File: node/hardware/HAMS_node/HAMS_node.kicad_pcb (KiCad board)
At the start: 2 copper layers, 47.5 x 50 mm, 45 parts, among them J1 Conn_01x02, J2 Conn_02x07_Odd_Even, J3 Conn_01x08, J4 Conn_01x04, J5 Conn_01x04, J6 Conn_01x04, J7 Conn_01x04, Q1 DMP3099L, SW1 TL3305BF100QG, SW2 JS202011SCQN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

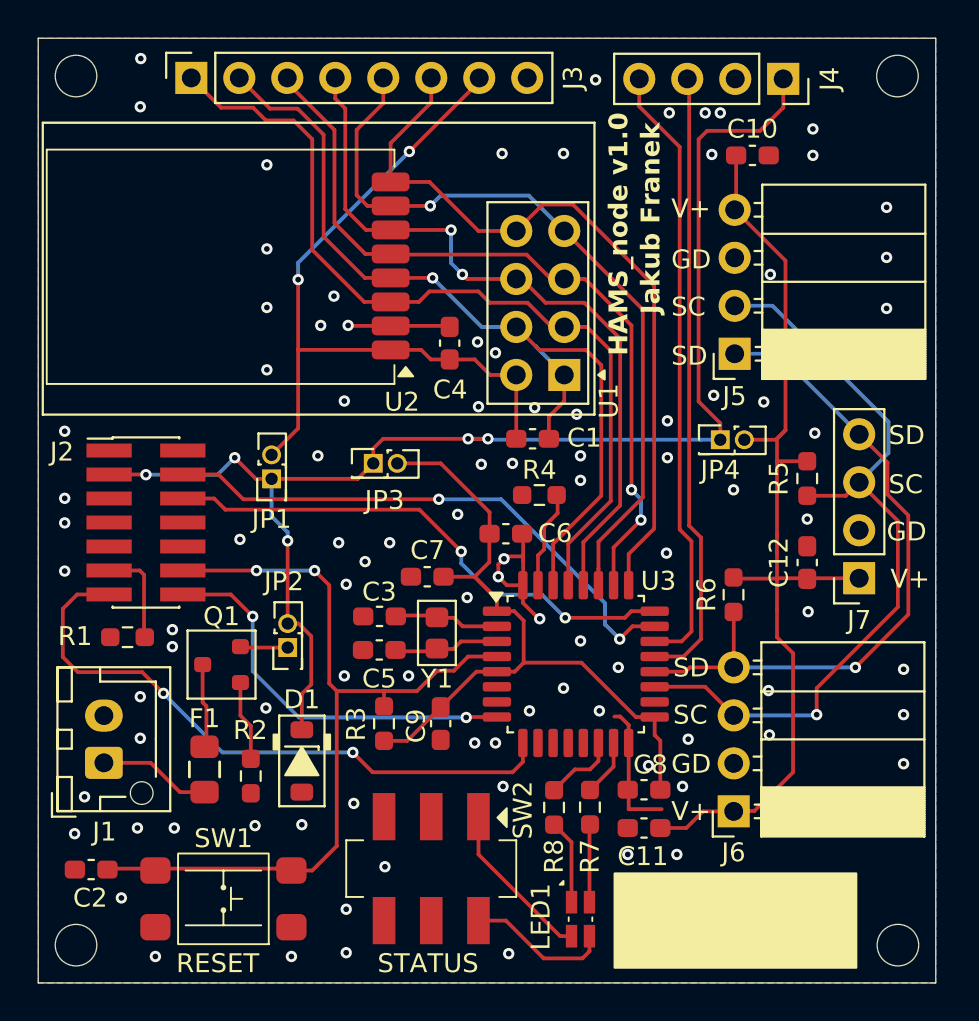
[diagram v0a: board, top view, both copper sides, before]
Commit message: Improve HAMS hub & node HW: schematic and PCB
Finalize hub and node PCB layouts & schematics.
Update task list.
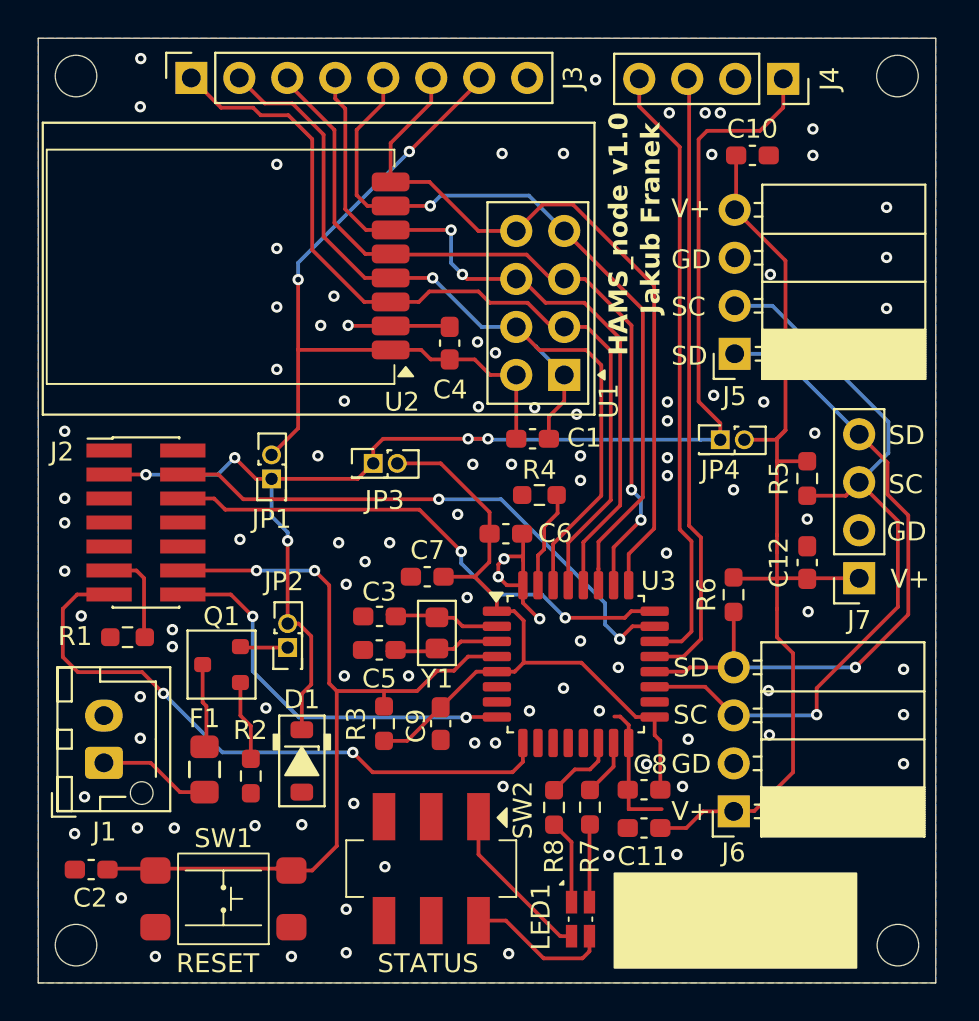
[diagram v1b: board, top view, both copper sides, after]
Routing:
- net GND: vias 95 -> 98
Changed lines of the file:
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@@
 	)
 	(via
-		(at 198.9 96.1)
+		(at 198.8 96.025)
 		(size 0.6)
 		(drill 0.3)
@@
 	)
 	(via
+		(at 199.9 76.85)
+		(size 0.6)
+		(drill 0.3)
+		(layers "F.Cu" "B.Cu")
+		(free yes)
+		(net 1)
+	)
+	(via
 		(at 211.5 71.9)
 		(size 0.6)
@@
 	)
 	(via
-		(at 191.7 80.1)
+		(at 191.65 80.15)
 		(size 0.6)
 		(drill 0.3)
@@
 	)
 	(via
+		(at 199.9 80.75)
+		(size 0.6)
+		(drill 0.3)
+		(layers "F.Cu" "B.Cu")
+		(free yes)
+		(net 1)
+	)
+	(via
 		(at 195.3 89.5)
 		(size 0.6)
@@
 	)
 	(via
-		(at 197.8 100.8)
+		(at 196.8 100.85)
 		(size 0.6)
 		(drill 0.3)
@@
 	)
 	(via
-		(at 178.7 68.75)
+		(at 179.225 68.725)
 		(size 0.6)
 		(drill 0.3)
@@
 	)
 	(via
+		(at 168.875 88.175)
+		(size 0.6)
+		(drill 0.3)
+		(layers "F.Cu" "B.Cu")
+		(free yes)
+		(net 1)
+	)
+	(via
 		(at 194.4 63.7)
 		(size 0.6)
@@
 	)
 	(via
-		(at 190.05 80.15)
+		(at 189.6 80.15)
 		(size 0.6)
 		(drill 0.3)
@@
 	)
 	(via
-		(at 178.7 64.3)
+		(at 179.225 64.275)
 		(size 0.6)
 		(drill 0.3)
@@
 	)
 	(via
-		(at 178.7 71.85)
+		(at 179.225 71.825)
 		(size 0.6)
 		(drill 0.3)
@@
 	)
 	(via
-		(at 178.7 75.15)
+		(at 179.225 75.125)
 		(size 0.6)
 		(drill 0.3)
@@
 	)
 	(segment
-		(start 170.35 85.77)
-		(end 171.97 85.77)
+		(start 172.2 86.175)
+		(end 172.2 88.875)
 		(width 0.2)
 		(layer "F.Cu")
@@
 	)
 	(segment
-		(start 171.97 85.77)
-		(end 172.2 86)
+		(start 171.795 85.77)
+		(end 172.2 86.175)
 		(width 0.2)
 		(layer "F.Cu")
@@
 	)
 	(segment
-		(start 172.2 86)
-		(end 172.2 88.875)
+		(start 170.35 85.77)
+		(end 171.795 85.77)
 		(width 0.2)
 		(layer "F.Cu")
@@
 	)
 	(segment
-		(start 183.885 70.285)
-		(end 181.702 68.102)
-		(width 0.2)
-		(layer "F.Cu")
-		(net 26)
-	)
-	(segment
 		(start 191.8995 72.88)
 		(end 193.1195 74.1)
@@
 	)
 	(segment
-		(start 181.702 62.702)
-		(end 180.325 61.325)
+		(start 181.702 68.102)
+		(end 181.702 62.702)
 		(width 0.2)
 		(layer "F.Cu")
@@
 	)
 	(segment
-		(start 181.702 68.102)
-		(end 181.702 62.702)
-		(width 0.2)
-		(layer "F.Cu")
-		(net 26)
-	)
-	(segment
 		(start 195.6 74.1)
 		(end 196.4 74.9)
@@
 	)
 	(segment
-		(start 180.325 61.325)
-		(end 178.865 61.325)
+		(start 185.25 70.285)
+		(end 183.885 70.285)
 		(width 0.2)
 		(layer "F.Cu")
@@
 	)
 	(segment
+		(start 181.702 62.702)
+		(end 180.05 61.05)
+		(width 0.2)
+		(layer "F.Cu")
+		(net 26)
+	)
+	(segment
 		(start 196.4 81.813928)
 		(end 193.85 84.363928)
@@
 	)
 	(segment
-		(start 177.24 59.7)
-		(end 177.21 59.73)
+		(start 178.59 61.05)
+		(end 177.24 59.7)
 		(width 0.2)
 		(layer "F.Cu")
@@
 	)
 	(segment
-		(start 185.25 70.285)
-		(end 183.885 70.285)
+		(start 183.885 70.285)
+		(end 181.702 68.102)
 		(width 0.2)
 		(layer "F.Cu")
@@
 	)
 	(segment
-		(start 178.865 61.325)
-		(end 177.24 59.7)
+		(start 180.05 61.05)
+		(end 178.59 61.05)
+		(width 0.2)
+		(layer "F.Cu")
+		(net 26)
+	)
+	(segment
+		(start 177.24 59.7)
+		(end 177.21 59.73)
 		(width 0.2)
 		(layer "F.Cu")
@@
 	)
 	(segment
-		(start 199.2 83.55)
-		(end 197.85 84.9)
+		(start 194.9 66.4)
+		(end 199.2 70.7)
 		(width 0.2)
 		(layer "F.Cu")
@@
 	)
 	(segment
-		(start 191.8995 67.8)
-		(end 193.2995 66.4)
+		(start 189.9 67.8)
+		(end 191.8995 67.8)
 		(width 0.2)
 		(layer "F.Cu")
@@
 	)
 	(segment
-		(start 194.9 66.4)
-		(end 199.2 70.7)
+		(start 185.25 63.15)
+		(end 187.4 61)
 		(width 0.2)
 		(layer "F.Cu")
@@
 	)
 	(segment
-		(start 189.9 67.8)
-		(end 191.8995 67.8)
+		(start 185.25 65.205)
+		(end 185.25 63.15)
 		(width 0.2)
 		(layer "F.Cu")
@@
 	)
 	(segment
-		(start 185.25 63.15)
-		(end 187.4 61)
+		(start 187.305 65.205)
+		(end 189.9 67.8)
 		(width 0.2)
 		(layer "F.Cu")
@@
 	)
 	(segment
-		(start 193.2995 66.4)
-		(end 194.9 66.4)
+		(start 187.4 61)
+		(end 187.4 59.7)
 		(width 0.2)
 		(layer "F.Cu")
@@
 	)
 	(segment
-		(start 185.25 65.205)
-		(end 185.25 63.15)
+		(start 191.8995 67.8)
+		(end 193.2995 66.4)
 		(width 0.2)
 		(layer "F.Cu")
@@
 	)
 	(segment
-		(start 187.305 65.205)
-		(end 189.9 67.8)
+		(start 185.25 65.205)
+		(end 187.305 65.205)
 		(width 0.2)
 		(layer "F.Cu")
@@
 	)
 	(segment
-		(start 187.4 61)
-		(end 187.4 59.7)
+		(start 193.2995 66.4)
+		(end 194.9 66.4)
 		(width 0.2)
 		(layer "F.Cu")
@@
 	)
 	(segment
-		(start 185.25 65.205)
-		(end 187.305 65.205)
+		(start 199.2 83.55)
+		(end 197.85 84.9)
 		(width 0.2)
 		(layer "F.Cu")
@@
 	)
 	(segment
+		(start 194.65 84.3)
+		(end 194.65 86.55)
+		(width 0.2)
+		(layer "F.Cu")
+		(net 29)
+	)
+	(segment
 		(start 194.4395 72.88)
 		(end 193.78 72.88)
@@
 	)
 	(segment
-		(start 176.275 61.275)
-		(end 174.7 59.7)
+		(start 186.745 71.555)
+		(end 185.25 71.555)
 		(width 0.2)
 		(layer "F.Cu")
@@
 	)
 	(segment
-		(start 178.65 61.95)
+		(start 178.375 61.675)
 		(end 177.975 61.275)
 		(width 0.2)
@@
 	)
 	(segment
-		(start 186.745 71.555)
-		(end 185.25 71.555)
+		(start 183.855 71.555)
+		(end 181.1 68.8)
 		(width 0.2)
 		(layer "F.Cu")
@@
 	)
 	(segment
-		(start 196.9 74.138419)
-		(end 196.9 82.1)
+		(start 176.275 61.275)
+		(end 174.7 59.7)
 		(width 0.2)
 		(layer "F.Cu")
@@
 	)
 	(segment
-		(start 183.855 71.555)
-		(end 181.1 68.8)
+		(start 181.1 68.8)
+		(end 181.1 62.9375)
 		(width 0.2)
 		(layer "F.Cu")
@@
 	)
 	(segment
-		(start 181.1 62.9375)
-		(end 180.1125 61.95)
+		(start 193.78 72.88)
+		(end 192.5 71.6)
 		(width 0.2)
 		(layer "F.Cu")
@@
 	)
 	(segment
-		(start 180.1125 61.95)
-		(end 178.65 61.95)
+		(start 196.9 74.138419)
+		(end 196.9 82.05)
 		(width 0.2)
 		(layer "F.Cu")
@@
 	)
 	(segment
-		(start 193.78 72.88)
-		(end 192.5 71.6)
+		(start 196.9 82.05)
+		(end 194.65 84.3)
 		(width 0.2)
 		(layer "F.Cu")
@@
 	)
 	(segment
-		(start 196.9 82.1)
-		(end 194.65 84.35)
+		(start 177.975 61.275)
+		(end 176.275 61.275)
 		(width 0.2)
 		(layer "F.Cu")
@@
 	)
 	(segment
-		(start 190.5 71.6)
-		(end 189.9 71)
+		(start 179.8375 61.675)
+		(end 178.375 61.675)
 		(width 0.2)
 		(layer "F.Cu")
@@
 	)
 	(segment
-		(start 194.65 84.35)
-		(end 194.65 86.55)
+		(start 190.5 71.6)
+		(end 189.9 71)
 		(width 0.2)
 		(layer "F.Cu")
@@
 	)
 	(segment
-		(start 181.1 68.8)
-		(end 181.1 62.9375)
-		(width 0.2)
-		(layer "F.Cu")
-		(net 29)
-	)
-	(segment
-		(start 177.975 61.275)
-		(end 176.275 61.275)
+		(start 181.1 62.9375)
+		(end 179.8375 61.675)
 		(width 0.2)
 		(layer "F.Cu")
@@
 		(polygon
 			(pts
-				(xy 166.95 77.67) (xy 166.875 62.145) (xy 177.575 62.145) (xy 177.65 77.67)
+				(xy 166.95 77.67) (xy 166.875 62.145) (xy 178.5 62.145) (xy 178.575 77.67)
 			)
 		)

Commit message: Improve HAMS hub HW: status button rework
Replace toggle switch with tactile switch for status button.
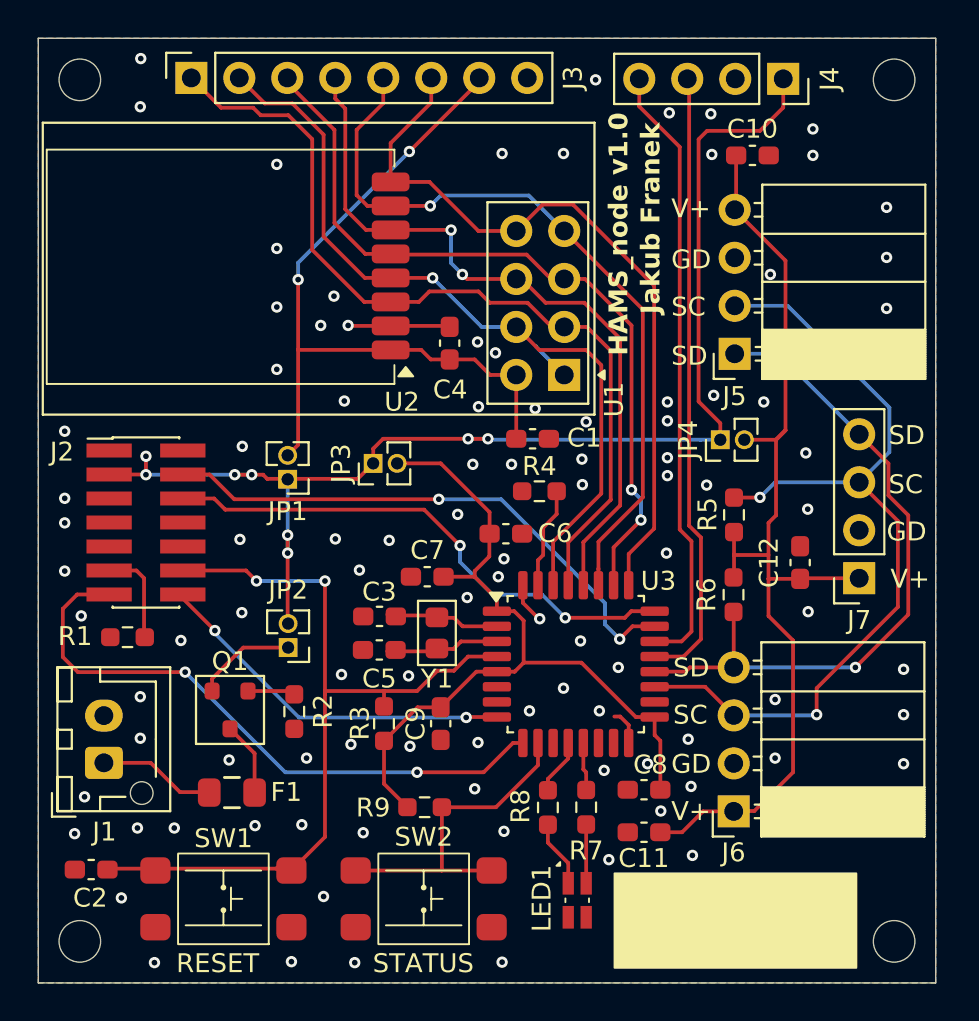
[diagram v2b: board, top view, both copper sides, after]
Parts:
- removed D1: 3.6 V (MMSZ5227B), PCM_Diode_SMD_Handsoldering_AKL:D_SOD-123_Zener
- added R9: 10 kOhm, Resistor_SMD:R_0603_1608Metric_Pad0.98x0.95mm_HandSolder, F.Cu at (187.1, 98.3)
- JP1, JP2, JP3, JP4: footprint Connector_PinHeader_1.27mm:PinHeader_2x01_P1.27mm_Vertical -> Connector_PinHeader_1.27mm:PinHeader_1x02_P1.27mm_Vertical
- SW2: value JS202011SCQN -> TL3305BF100QG; footprint Personal_SamacSys:JS202011SCQN -> Personal_Switches:E-Switch_TL3305BF100QG_Tactile_SPST
- moved R5 4.33 mm to (203.4, 82.8), turned to -90 degrees
- moved R2 4.12 mm to (180.2, 93.2)
- moved Q1 2.44 mm to (176.8, 93.2), turned to -90 degrees
- moved F1 1.90 mm to (176.8, 97.5), turned to 0 degrees
- moved SW2 1.65 mm to (187.0, 103.2)
- moved LED1 1.02 mm to (195.1, 103.1)
- moved JP1 0.85 mm to (179.8, 80.9), turned to 180 degrees
- moved C12 0.38 mm to (206.9, 85.3)
- moved R8 0.33 mm to (193.6, 98.3)
- moved H2 0.28 mm to (168.8, 59.8)
- moved H1 0.28 mm to (168.8, 105.4)
- moved H3 0.28 mm to (211.9, 105.4)
- moved H4 0.27 mm to (211.9, 59.8)
- moved C11 0.22 mm to (198.7, 99.6)
- moved R7 0.20 mm to (195.6, 98.3)
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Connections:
- LED1 pad 2: Net-(LED1-CATHODE_RED) -> GND
- LED1 pad 3: Net-(LED1-CATHODE_GREEN) -> GND
- SW2 pad 1: Net-(LED1-CATHODE_RED) -> GND
- SW2 pad 2: GND -> /BTN_STATUS
- U3 pad 10: unconnected-(U3-PA4-Pad10) -> /BTN_STATUS
- U3 pad 12: unconnected-(U3-PA6-Pad12) -> /LED_RED
- U3 pad 13: unconnected-(U3-PA7-Pad13) -> /LED_GREEN
- U3 pad 14: /LED_RED -> unconnected-(U3-PB0-Pad14)
- U3 pad 15: /LED_GREEN -> unconnected-(U3-PB1-Pad15)
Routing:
- net /BTN_STATUS: track 0.00 -> 17.7 mm
- net GND: track 26.2 -> 11.9 mm, vias 98 -> 100
- net Net-(LED1-CATHODE_RED): track 9.07 -> 0.00 mm
- net Net-(LED1-CATHODE_GREEN): track 8.16 -> 0.00 mm
- net /I2C_SCL: track 42.0 -> 46.2 mm, vias 1 -> 2
- net /VDD_MCU: track 38.7 -> 42.7 mm
- net VDD: track 73.4 -> 69.4 mm, vias 5 -> 8
- net Net-(JP2-A): track 2.52 -> 5.58 mm
- net /VDD_SENSOR: track 52.6 -> 54.4 mm
- net /VCP_TX: track 21.0 -> 19.5 mm
- net Net-(Q1-G): track 3.73 -> 2.52 mm
- net /LED_RED: track 3.94 -> 2.95 mm
- net /VCP_RX: track 33.4 -> 32.8 mm
- net Net-(Q1-D): track 4.47 -> 3.91 mm
- net Net-(LED1-ANODE_GREEN): track 3.62 -> 3.11 mm

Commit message: Improve HAMS node & hub HW: PCB update
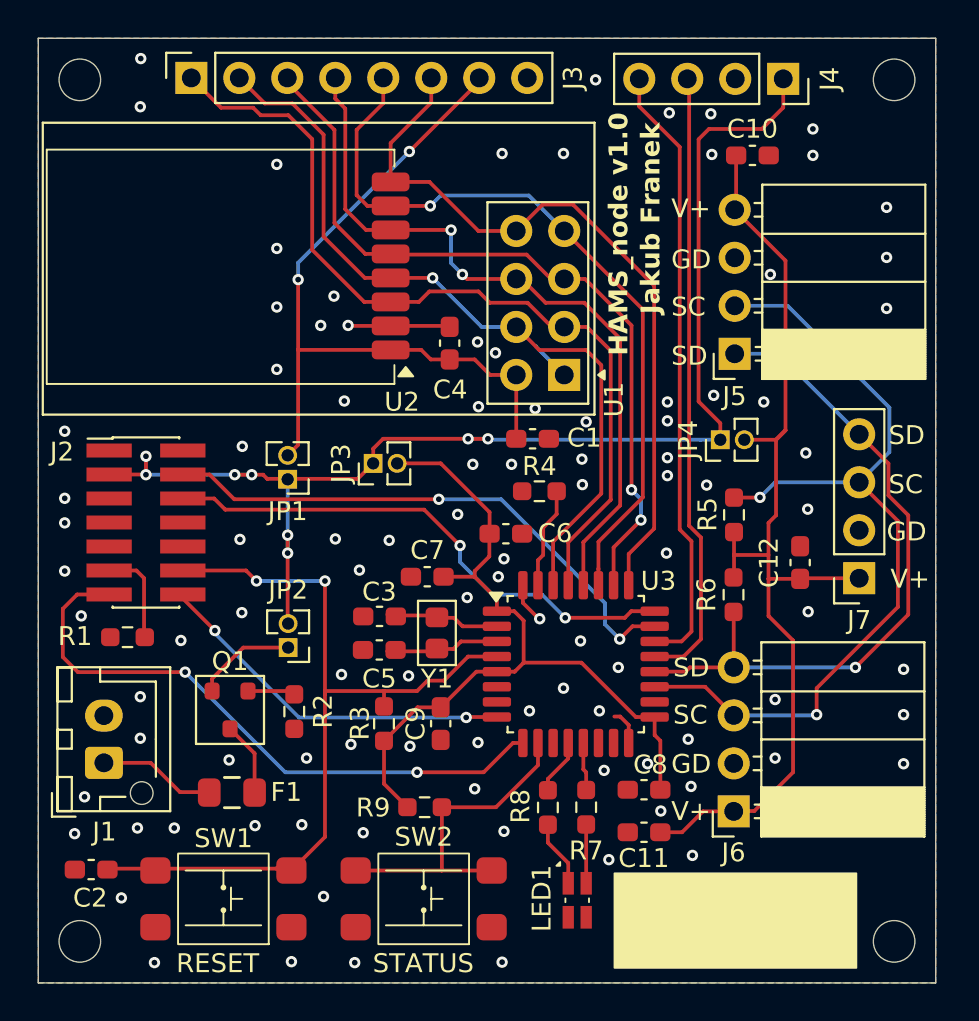
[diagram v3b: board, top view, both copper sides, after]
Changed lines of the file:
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@@
+	)
+	(segment
+		(start 187.2 91.6)
+		(end 188.075 91.6)
+		(width 0.2)
+		(layer "F.Cu")
+		(net 7)
 	)
 	(segment
@@
 	)
 	(segment
-		(start 188.6 91.075)
+		(start 184.9 92.15)
+		(end 186.65 92.15)
+		(width 0.2)
+		(layer "F.Cu")
+		(net 7)
+	)
+	(segment
+		(start 186.65 92.15)
+		(end 187.2 91.6)
+		(width 0.2)
+		(layer "F.Cu")
+		(net 7)
+	)
+	(segment
+		(start 188.075 91.6)
 		(end 189.35 90.325)
 		(width 0.2)
@@
 	)
 	(segment
-		(start 184.9 92.15)
-		(end 186.65 92.15)
+		(start 189.35 90.325)
+		(end 190.875 90.325)
 		(width 0.2)
 		(layer "F.Cu")
@@
 	)
 	(segment
-		(start 189.35 90.325)
-		(end 190.875 90.325)
-		(width 0.2)
-		(layer "F.Cu")
-		(net 7)
-	)
-	(segment
 		(start 178.15 86.325)
 		(end 177.595 85.77)
@@
 	)
 	(segment
-		(start 187.725 91.075)
-		(end 188.6 91.075)
-		(width 0.2)
-		(layer "F.Cu")
-		(net 7)
-	)
-	(segment
 		(start 181.775 92.325)
 		(end 181.775 99.875)
-		(width 0.2)
-		(layer "F.Cu")
-		(net 7)
-	)
-	(segment
-		(start 186.65 92.15)
-		(end 187.725 91.075)
 		(width 0.2)
 		(layer "F.Cu")
@@
 	)
 	(segment
-		(start 201.55 62.95)
-		(end 202 62.5)
+		(start 202.1 62.4)
+		(end 204.9 62.4)
 		(width 0.2)
 		(layer "F.Cu")
@@
 	)
 	(segment
+		(start 184.33 80.1)
+		(end 184.33 79.32)
+		(width 0.2)
+		(layer "F.Cu")
+		(net 8)
+	)
+	(segment
+		(start 179.8 83.9)
+		(end 179.8 84.85)
+		(width 0.2)
+		(layer "F.Cu")
+		(net 8)
+	)
+	(segment
+		(start 172.29 80.69)
+		(end 172.3 80.7)
+		(width 0.2)
+		(layer "F.Cu")
+		(net 8)
+	)
+	(segment
+		(start 178.72 80.92)
+		(end 183.51 80.92)
+		(width 0.2)
+		(layer "F.Cu")
+		(net 8)
+	)
+	(segment
+		(start 202.7 77.975)
+		(end 201.55 76.825)
+		(width 0.2)
+		(layer "F.Cu")
+		(net 8)
+	)
+	(segment
+		(start 172.3 80.7)
+		(end 172.3 79.725)
+		(width 0.2)
+		(layer "F.Cu")
+		(net 8)
+	)
+	(segment
+		(start 179.8 88.555)
+		(end 179.825 88.58)
+		(width 0.2)
+		(layer "F.Cu")
+		(net 8)
+	)
+	(segment
+		(start 179.8 84.85)
+		(end 179.8 88.555)
+		(width 0.2)
+		(layer "F.Cu")
+		(net 8)
+	)
+	(segment
+		(start 201.55 76.825)
+		(end 201.55 62.95)
+		(width 0.2)
+		(layer "F.Cu")
+		(net 8)
+	)
+	(segment
+		(start 202.7 78.85)
+		(end 202.7 77.975)
+		(width 0.2)
+		(layer "F.Cu")
+		(net 8)
+	)
+	(segment
+		(start 183.51 80.92)
+		(end 184.33 80.1)
+		(width 0.2)
+		(layer "F.Cu")
+		(net 8)
+	)
+	(segment
+		(start 184.85 78.8)
+		(end 189.35 78.8)
+		(width 0.2)
+		(layer "F.Cu")
+		(net 8)
+	)
+	(segment
+		(start 170.35 80.69)
+		(end 172.29 80.69)
+		(width 0.2)
+		(layer "F.Cu")
+		(net 8)
+	)
+	(segment
+		(start 204.9 62.4)
+		(end 206.03 61.27)
+		(width 0.2)
+		(layer "F.Cu")
+		(net 8)
+	)
+	(segment
 		(start 206.03 61.27)
 		(end 206.03 59.75)
@@
 	)
 	(segment
-		(start 184.33 80.1)
-		(end 184.33 79.32)
-		(width 0.2)
-		(layer "F.Cu")
-		(net 8)
-	)
-	(segment
-		(start 179.8 83.9)
-		(end 179.8 84.85)
-		(width 0.2)
-		(layer "F.Cu")
-		(net 8)
-	)
-	(segment
-		(start 172.29 80.69)
-		(end 172.3 80.7)
-		(width 0.2)
-		(layer "F.Cu")
-		(net 8)
-	)
-	(segment
-		(start 202 62.5)
-		(end 204.8 62.5)
-		(width 0.2)
-		(layer "F.Cu")
-		(net 8)
-	)
-	(segment
-		(start 178.72 80.92)
-		(end 183.51 80.92)
-		(width 0.2)
-		(layer "F.Cu")
-		(net 8)
-	)
-	(segment
-		(start 172.3 80.7)
-		(end 172.3 79.725)
-		(width 0.2)
-		(layer "F.Cu")
-		(net 8)
-	)
-	(segment
-		(start 179.8 88.555)
-		(end 179.825 88.58)
-		(width 0.2)
-		(layer "F.Cu")
-		(net 8)
-	)
-	(segment
-		(start 201.55 76.825)
-		(end 201.55 62.95)
-		(width 0.2)
-		(layer "F.Cu")
-		(net 8)
-	)
-	(segment
-		(start 179.8 84.85)
-		(end 179.8 88.555)
-		(width 0.2)
-		(layer "F.Cu")
-		(net 8)
-	)
-	(segment
-		(start 183.51 80.92)
-		(end 184.33 80.1)
-		(width 0.2)
-		(layer "F.Cu")
-		(net 8)
-	)
-	(segment
-		(start 184.85 78.8)
-		(end 189.35 78.8)
-		(width 0.2)
-		(layer "F.Cu")
-		(net 8)
-	)
-	(segment
-		(start 202.7 78.85)
-		(end 202.7 77.975)
-		(width 0.2)
-		(layer "F.Cu")
-		(net 8)
-	)
-	(segment
-		(start 170.35 80.69)
-		(end 172.29 80.69)
-		(width 0.2)
-		(layer "F.Cu")
-		(net 8)
-	)
-	(segment
-		(start 202.7 77.975)
-		(end 201.55 76.825)
-		(width 0.2)
-		(layer "F.Cu")
-		(net 8)
-	)
-	(segment
-		(start 204.8 62.5)
-		(end 206.03 61.27)
-		(width 0.2)
-		(layer "F.Cu")
-		(net 8)
-	)
-	(segment
 		(start 190.4 78.8)
 		(end 189.35 78.8)
@@
 		(width 0.2)
 		(layer "F.Cu")
+		(net 8)
+	)
+	(segment
+		(start 201.55 62.95)
+		(end 202.1 62.4)
+		(width 0.2)
+		(layer "F.Cu")

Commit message: Improve HAMS node & hub HW: PCB update
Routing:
- net /I2C_SCL: track 46.2 -> 50.0 mm, vias 2 -> 4
- net /SWCLK: track 28.6 -> 32.1 mm, vias 2 -> 4
- net /SWDIO: track 29.9 -> 32.7 mm, vias 2 -> 4
- net /SPI_MOSI: track 39.5 -> 42.3 mm, vias 2 -> 4
- net /VCP_TX: track 19.5 -> 22.1 mm, vias 2 -> 4
- net /NRST: track 44.1 -> 46.4 mm, vias 2 -> 4
- net /VDD_nRF24: track 39.3 -> 41.6 mm, vias 2 -> 4
- net /VCP_RX: track 32.8 -> 35.0 mm, vias 2 -> 4
- net /SPI_SCK: track 41.9 -> 43.5 mm, vias 2 -> 4
- net /nRF24_CSN: track 41.6 -> 42.7 mm, vias 1 -> 2
- net /I2C_SDA: track 36.8 -> 37.9 mm, vias 1 -> 2
- net /SPI_MISO: track 40.5 -> 41.4 mm, vias 1 -> 2
- net /nRF24_IRQ: track 40.5 -> 41.2 mm
